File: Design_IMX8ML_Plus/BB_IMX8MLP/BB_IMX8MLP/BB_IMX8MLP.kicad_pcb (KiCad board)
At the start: 2 copper layers, 125 x 100 mm, 134 parts, among them J1 DF40C-100DP-0.4V_51_, J10 Barrel_Jack, J11 SIM_Card, J2 DF40C-100DP-0.4V_51_, J3 DF40C-100DP-0.4V_51_, J4 DF40C-100DP-0.4V_51_, J5 RJ45_Amphenol_RJMG1BD3B8K1ANR, J6 RJ45_Amphenol_RJMG1BD3B8K1ANR, J7 HDMI_A, J8 Bus_PCI_Express_Mini, J9 GSB311231HR, P1 USB_C_Plug, Q1 PMDT290UCE, Q2 NTMFS5C670NLT1G, Q3 NTMFS5C670NLT1G, Q4 PMDT290UCE, SW1 Power ON/OFF, SW2 RESET, SW3 RECOVERY, U1 KSZ9131RNXI, U10 PCMF3USB3S, U2 HDMI2C1-14HDS, U3 USB5744_2G, U4 LTC4368IDD-1_PBF, U5 AOZ2261AQI-15, U6 NCV4274CST50T3G, U7 AOZ2261AQI-15, U8 LTC2954CDDB-1-TRMPBF, U9 PCMF3USB3S, Y1 25MHz

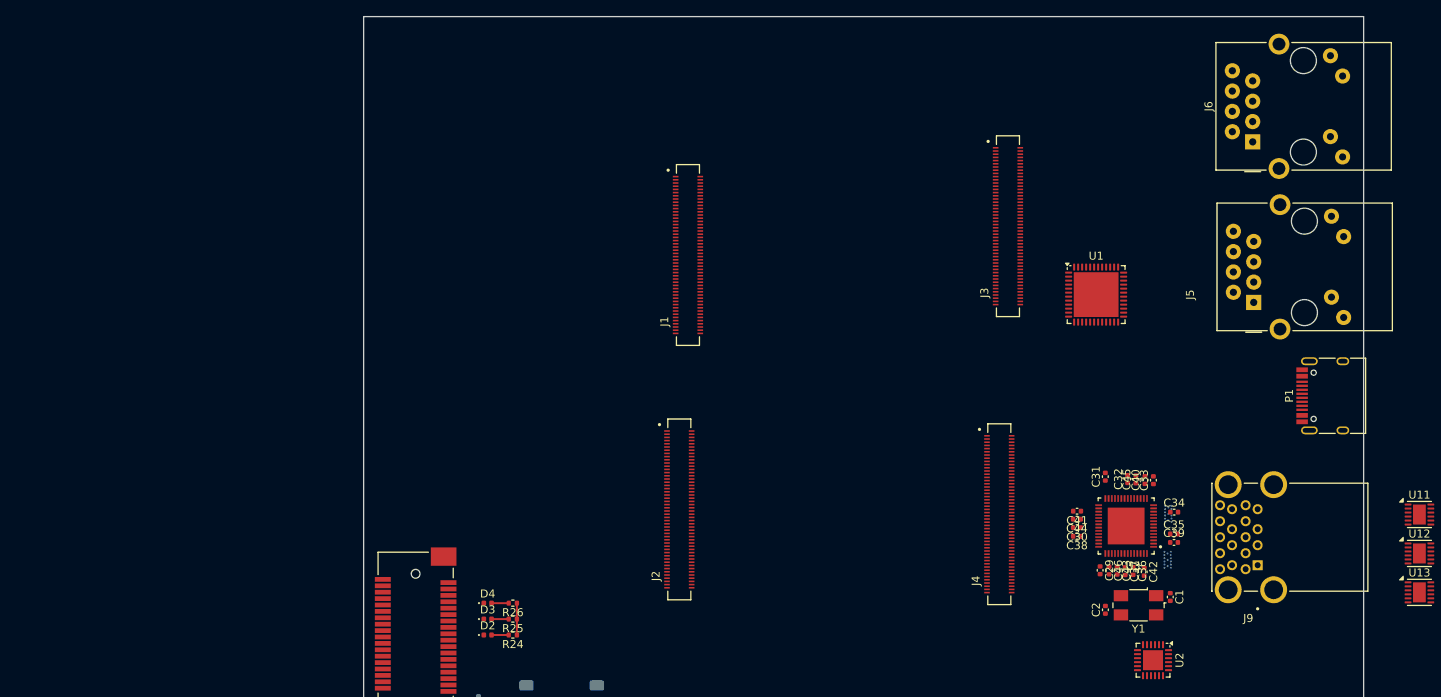
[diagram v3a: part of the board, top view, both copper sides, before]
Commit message: improving Ethernet, USB and Camera inteface
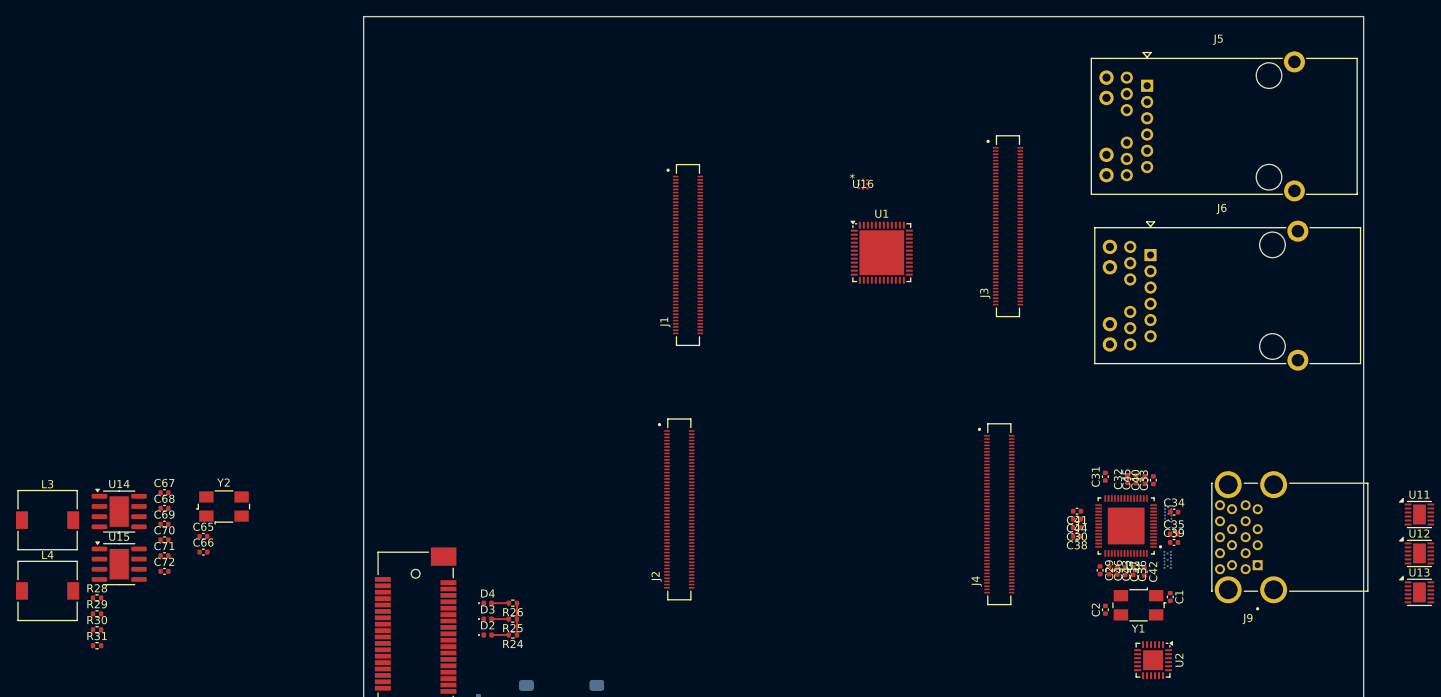
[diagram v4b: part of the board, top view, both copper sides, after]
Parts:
- removed P1: USB_C_Plug, Connector_USB:USB_C_Receptacle_HRO_TYPE-C-31-M-12
- added C65: 12Pf, Capacitor_SMD:C_0402_1005Metric, F.Cu at (50.0, 115.0)
- added C66: 12Pf, Capacitor_SMD:C_0402_1005Metric, F.Cu at (50.0, 116.9)
- added C67: 47uF, Capacitor_SMD:C_0402_1005Metric, F.Cu at (45.1, 109.5)
- added C68: 100pF, Capacitor_SMD:C_0402_1005Metric, F.Cu at (45.1, 111.5)
- added C69: 22uF, Capacitor_SMD:C_0402_1005Metric, F.Cu at (45.1, 113.4)
- added C70: 47uF, Capacitor_SMD:C_0402_1005Metric, F.Cu at (45.1, 115.4)
- added C71: 100pF, Capacitor_SMD:C_0402_1005Metric, F.Cu at (45.1, 117.4)
- added C72: 22uF, Capacitor_SMD:C_0402_1005Metric, F.Cu at (45.1, 119.3)
- added L3: 2.2uH_12A, Inductor_SMD:L_7.3x7.3_H3.5, F.Cu at (30.5, 112.9)
- added L4: 2.2uH_12A, Inductor_SMD:L_7.3x7.3_H3.5, F.Cu at (30.5, 121.8)
- added R28: 330K, Resistor_SMD:R_0402_1005Metric, F.Cu at (36.7, 122.7)
- added R29: 150K, Resistor_SMD:R_0402_1005Metric, F.Cu at (36.7, 124.7)
- added R30: 150K, Resistor_SMD:R_0402_1005Metric, F.Cu at (36.7, 126.7)
- added R31: 150K, Resistor_SMD:R_0402_1005Metric, F.Cu at (36.7, 128.6)
- added U14: ~, Package_SO:SOIC-8-1EP_3.9x4.9mm_P1.27mm_EP2.41x3.81mm, F.Cu at (39.4, 111.9)
- added U15: ~, Package_SO:SOIC-8-1EP_3.9x4.9mm_P1.27mm_EP2.41x3.81mm, F.Cu at (39.4, 118.5)
- added U16: ~, _W_SBC:MICROPAK8_1P6X1P6_ONS, F.Cu at (132.4, 71.0)
- added Y2: 25MHz, Crystal:Crystal_SMD_0603-4Pin_6.0x3.5mm, F.Cu at (52.5, 111.2)
- C17: value 47uF -> 4.7uF
- C18, C19: value 47uF -> 100nF
- C7, C8: value 100nF -> 47uF
- C9: value 4.7uF -> 47uF
- J5, J6: value RJ45_Amphenol_RJMG1BD3B8K1ANR -> RJ45_JK0654219; footprint Connector_RJ:RJ45_Amphenol_RJMG1BD3B8K1ANR -> Connector_RJ:RJ45_Pulse_JK0654219NL_Horizontal
- R1: value 47K -> 100K
- R2: value 8.87K -> 100K
- R4: value 100K -> 47K
- R5: value 100K -> 8.87K
- R6: value 510K -> 100K
- R8: value 100K -> 510K
- moved J5 30.2 mm to (167.9, 58.6), turned to 0 degrees
- moved U1 27.3 mm to (134.8, 79.5)
- moved J6 19.1 mm to (168.4, 79.8), turned to 0 degrees
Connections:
- C17 pad 1: VDD_SYS -> /power_unit/power_5v/+V_STB
- C18 pad 1: VDD_SYS -> Net-(U5B-BST)
- C18 pad 2: GND -> Net-(C18-Pad2)
- C19 pad 1: VDD_SYS -> Net-(U5A-SS)
- C21 pad 1: VDD_SYS -> +3.3V
- C22 pad 1: VDD_SYS -> +3.3V
- C23 pad 1: VDD_SYS -> +3.3V
- C24 pad 1: VDD_SYS -> +3.3V
- C25 pad 1: /power_unit/+V_STB -> /power_unit/power_3V3_1V8_1V2/+V_STB
- C7 pad 1: Net-(U5B-BST) -> VDD_SYS
- C7 pad 2: Net-(C7-Pad2) -> GND
- C8 pad 1: Net-(U5A-SS) -> VDD_SYS
- C9 pad 1: /power_unit/+V_STB -> VDD_SYS
- J5 pad 13: unconnected-(J5-SHIELD-Pad13) -> /Ethernet/ETH2_LED2
- J6 pad 13: unconnected-(J6-SHIELD-Pad13) -> ETH1_LED2
- J8 pad 11: unconnected-(J8-REFCLK--Pad11) -> PCIE_REF_PAD_CLK_N
- J8 pad 13: unconnected-(J8-REFCLK+-Pad13) -> PCIE_REF_PAD_CLK_P
- J8 pad 23: unconnected-(J8-PERn0-Pad23) -> PCIE_RXN_N
- J8 pad 25: unconnected-(J8-PERp0-Pad25) -> PCIE_RXN_P
- J8 pad 28: unconnected-(J8-+1V5-Pad28) -> Net-(J8-+1V5-Pad28)
- J8 pad 31: unconnected-(J8-PETn0-Pad31) -> PCIE_TXN_N
- J8 pad 33: unconnected-(J8-PETp0-Pad33) -> PCIE_TXN_P
- J8 pad 36: USBDN_D3- -> USBH4_D-
- J8 pad 38: USBDN_D3+ -> USBH4_D+
- J8 pad 48: unconnected-(J8-+1V5-Pad48) -> Net-(J8-+1V5-Pad28)
- J8 pad 6: unconnected-(J8-+1V5-Pad6) -> Net-(J8-+1V5-Pad28)
- J9 pad 16: unconnected-(J9B-GND_DRAIN_2-Pad16) -> GND
- L1 pad 2: Net-(C7-Pad2) -> Net-(C18-Pad2)
- L2 pad 1: VDD_SYS -> +3.3V
- Q1 pad 4: /power_unit/+V5_STB -> /power_unit/power_5v/+V5_STB
- Q4 pad 4: /power_unit/+V5_STB -> /power_unit/power_3V3_1V8_1V2/+V5_STB
- R1 pad 1: VDD_SYS -> /power_unit/power_5v/5V_EN
- R1 pad 2: /power_unit/FB_5V -> Net-(Q1B-GP)
- R16 pad 1: /power_unit/5V_EN -> /power_unit/power_3V3_1V8_1V2/5V_EN
- R17 pad 1: /power_unit/+V5_STB -> /power_unit/power_3V3_1V8_1V2/+V5_STB
- R19 pad 1: VDD_SYS -> +3.3V
- R19 pad 2: /power_unit/FB_5V -> /power_unit/power_3V3_1V8_1V2/FB_5V
- R2 pad 1: /power_unit/FB_5V -> /power_unit/power_5v/+V5_STB
- R2 pad 2: GND -> Net-(Q1B-GP)
- R20 pad 1: /power_unit/FB_5V -> /power_unit/power_3V3_1V8_1V2/FB_5V
- R22 pad 1: /power_unit/+V_SUPPLY_FILT -> /power_unit/power_3V3_1V8_1V2/+V_SUPPLY_FILT
- R23 pad 1: /power_unit/+V_STB -> /power_unit/power_3V3_1V8_1V2/+V_STB
- R3 pad 1: /power_unit/+V_STB -> Net-(Q1B-DP)
- R3 pad 2: Net-(U5B-PGOOD) -> GND
- R4 pad 1: Net-(U5A-*PFM) -> VDD_SYS
- R4 pad 2: GND -> /power_unit/power_5v/FB_5V
- R5 pad 1: Net-(Q1B-DP) -> /power_unit/power_5v/FB_5V
- R6 pad 1: /power_unit/+V_SUPPLY_FILT -> Net-(U5A-*PFM)
- R6 pad 2: Net-(U5A-TON) -> GND
- R8 pad 1: /power_unit/+V5_STB -> /power_unit/power_5v/+V_SUPPLY_FILT
- R8 pad 2: Net-(Q1B-GP) -> Net-(U5A-TON)
- R9 pad 1: /power_unit/5V_EN -> /power_unit/power_5v/+V_STB
- R9 pad 2: Net-(Q1B-GP) -> Net-(U5B-PGOOD)
- U1 pad 1: unconnected-(U1B-AVDDH-Pad1) -> Net-(U1B-AVDDH-Pad1)
- U1 pad 10: unconnected-(U1A-TXRXP_D-Pad10) -> /Ethernet/ETH2_MDI3+
- U1 pad 11: unconnected-(U1A-TXRXM_D-Pad11) -> /Ethernet/ETH2_MDI3-
- U1 pad 12: unconnected-(U1B-AVDDH-Pad12) -> Net-(U1B-AVDDH-Pad1)
- U1 pad 15: unconnected-(U1A-LED2/PHYAD1-Pad15) -> /Ethernet/ETH2_LED2
- U1 pad 17: unconnected-(U1A-LED1/PME_N1//PHYAD0-Pad17) -> /Ethernet/ETH2_LED1
- U1 pad 19: unconnected-(U1A-TXD0-Pad19) -> ENET_TD0
- U1 pad 2: unconnected-(U1A-TXRXP_A-Pad2) -> /Ethernet/ETH2_MDI0+
- U1 pad 20: unconnected-(U1A-TXD1-Pad20) -> ENET_TD1
- U1 pad 21: unconnected-(U1A-TXD2-Pad21) -> ENET_TD2
- U1 pad 22: unconnected-(U1A-TXD3-Pad22) -> ENET_TD3
- U1 pad 24: unconnected-(U1A-TXC-Pad24) -> ENET_TXC
- U1 pad 25: unconnected-(U1A-TX_CTL-Pad25) -> ENET_TX_CTL
- U1 pad 27: unconnected-(U1A-RXD3/MODE3-Pad27) -> ENET_RD3
- U1 pad 28: unconnected-(U1A-RXD2/MODE2-Pad28) -> ENET_RD2
- U1 pad 3: unconnected-(U1A-TXRXM_A-Pad3) -> /Ethernet/ETH2_MDI0-
- U1 pad 31: unconnected-(U1A-RXD1/MODE1-Pad31) -> ENET_RD1
- U1 pad 32: unconnected-(U1A-RXD0/MODE0-Pad32) -> ENET_RD0
- U1 pad 33: unconnected-(U1A-RX_CTL/CLK125_EN-Pad33) -> ENET_RX_CTL
- U1 pad 35: unconnected-(U1A-RXC/PHYAD2-Pad35) -> ENET_RXC
- U1 pad 36: unconnected-(U1A-MDC-Pad36) -> ENET_MDC
- U1 pad 37: unconnected-(U1A-MDIO-Pad37) -> ENET_MDIO
- U1 pad 4: unconnected-(U1B-AVDDL-Pad4) -> Net-(U1B-AVDDL-Pad4)
- U1 pad 42: unconnected-(U1A-RESET_N-Pad42) -> CTRL_RESET
- U1 pad 45: unconnected-(U1A-XO-Pad45) -> Net-(U1A-XO)
- U1 pad 46: unconnected-(U1A-XI-Pad46) -> Net-(U1A-XI)
- U1 pad 5: unconnected-(U1A-TXRXP_B-Pad5) -> /Ethernet/ETH2_MDI1+
- U1 pad 6: unconnected-(U1A-TXRXM_B-Pad6) -> /Ethernet/ETH2_MDI1-
- U1 pad 7: unconnected-(U1A-TXRXP_C-Pad7) -> /Ethernet/ETH2_MDI2+
- U1 pad 8: unconnected-(U1A-TXRXM_C-Pad8) -> /Ethernet/ETH2_MDI2-
- U1 pad 9: unconnected-(U1B-AVDDL-Pad9) -> Net-(U1B-AVDDL-Pad4)
- U10 pad A1: /USB/usb_connectors/USBDN_D2- -> USBH2_D-
- U10 pad A2: /USB/usb_connectors/USBDN_D2+ -> USBH2_D+
- U10 pad A3: /USB/usb_connectors/USB_SSRX_DN2- -> USBH2_SSRX-
- U10 pad A4: /USB/usb_connectors/USB_SSRX_DN2+ -> USBH2_SSRX+
- U10 pad A5: /USB/usb_connectors/USB_SSTX_DN2- -> USBH2_SSTX-
- U10 pad A6: /USB/usb_connectors/USB_SSTX_DN2+ -> USBH2_SSTX+
- U3 pad 1: /USB/USBDN_D1+ -> unconnected-(U3-USB2DN_DP1/PRT_DIS_P1-Pad1)
- U3 pad 10: /USB/USB_SSTX_DN2+ -> USBH2_SSTX+
- U3 pad 11: /USB/USB_SSTX_DN2- -> USBH2_SSTX-
- U3 pad 13: /USB/USB_SSRX_DN2+ -> USBH2_SSRX+
- U3 pad 14: /USB/USB_SSRX_DN2- -> USBH2_SSRX-
- U3 pad 17: USBDN_D3+ -> USBH3_D+
- U3 pad 18: USBDN_D3- -> USBH3_D-
- U3 pad 19: unconnected-(U3-USB3DN_TXDP3-Pad19) -> USBH3_SSTX+
- U3 pad 2: /USB/USBDN_D1- -> unconnected-(U3-USB2DN_DM1/PRT_DIS_M1-Pad2)
- U3 pad 20: unconnected-(U3-USB3DN_TXDM3-Pad20) -> USBH3_SSTX-
- U3 pad 22: unconnected-(U3-USB3DN_RXDP3-Pad22) -> USBH3_SSRX+
- U3 pad 23: unconnected-(U3-USB3DN_RXDM3-Pad23) -> USBH3_SSRX-
- U3 pad 24: /USB/USBDN_D4+ -> USBH4_D+
- U3 pad 25: /USB/USBDN_D4- -> USBH4_D-
- U3 pad 3: /USB/USB_SSTX_DN1+ -> unconnected-(U3-USB3DN_TXDP1-Pad3)
- U3 pad 34: unconnected-(U3-PRT_CTL3-Pad34) -> USBH3_PRT_CTL
- U3 pad 35: unconnected-(U3-PRT_CTL2-Pad35) -> USBH2_PRT_CTL
- U3 pad 4: /USB/USB_SSTX_DN1- -> unconnected-(U3-USB3DN_TXDM1-Pad4)
- U3 pad 6: /USB/USB_SSRX_DN1+ -> unconnected-(U3-USB3DN_RXDP1-Pad6)
- U3 pad 7: /USB/USB_SSRX_DN1- -> unconnected-(U3-USB3DN_RXDM1-Pad7)
- U3 pad 8: /USB/USBDN_D2+ -> USBH2_D+
- U3 pad 9: /USB/USBDN_D2- -> USBH2_D-
- U5 pad 10: Net-(C7-Pad2) -> Net-(C18-Pad2)
- U5 pad 11: Net-(C7-Pad2) -> Net-(C18-Pad2)
- U5 pad 16: Net-(C7-Pad2) -> Net-(C18-Pad2)
- U5 pad 17: Net-(C7-Pad2) -> Net-(C18-Pad2)
- U5 pad 18: Net-(C7-Pad2) -> Net-(C18-Pad2)
- U5 pad 21: /power_unit/+V_STB -> /power_unit/power_5v/+V_STB
- U5 pad 5: /power_unit/FB_5V -> /power_unit/power_5v/FB_5V
- U5 pad 7: /power_unit/+V_SUPPLY_FILT -> /power_unit/power_5v/+V_SUPPLY_FILT
- U5 pad 8: /power_unit/+V_SUPPLY_FILT -> /power_unit/power_5v/+V_SUPPLY_FILT
- U5 pad 9: /power_unit/+V_SUPPLY_FILT -> /power_unit/power_5v/+V_SUPPLY_FILT
- U7 pad 21: /power_unit/+V_STB -> /power_unit/power_3V3_1V8_1V2/+V_STB
- U7 pad 5: /power_unit/FB_5V -> /power_unit/power_3V3_1V8_1V2/FB_5V
- U7 pad 7: /power_unit/+V_SUPPLY_FILT -> /power_unit/power_3V3_1V8_1V2/+V_SUPPLY_FILT
- U7 pad 8: /power_unit/+V_SUPPLY_FILT -> /power_unit/power_3V3_1V8_1V2/+V_SUPPLY_FILT
- U7 pad 9: /power_unit/+V_SUPPLY_FILT -> /power_unit/power_3V3_1V8_1V2/+V_SUPPLY_FILT
- U8 pad 3: Net-(SW1-A) -> /power_unit/+V5_STB
- U9 pad A1: /USB/usb_connectors/USBDN_D1- -> USBH3_D-
- U9 pad A2: /USB/usb_connectors/USBDN_D1+ -> USBH3_D+
- U9 pad A3: /USB/usb_connectors/USB_SSTX_DN1- -> USBH3_SSTX-
- U9 pad A4: /USB/usb_connectors/USB_SSTX_DN1+ -> USBH3_SSTX+
- U9 pad A5: /USB/usb_connectors/USB_SSRX_DN1- -> USBH3_SSRX-
- U9 pad A6: /USB/usb_connectors/USB_SSRX_DN1+ -> USBH3_SSRX+
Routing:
- net GND: track 16.8 -> 30.5 mm
- net Net-(C7-Pad2): track 13.7 -> 0.00 mm
- net /power_unit/FB_5V: track 7.73 -> 0.00 mm, vias 1 -> 0
- net Net-(Q1B-GP): track 8.71 -> 16.4 mm, vias 0 -> 1
- net /power_unit/+V_STB: track 2.70 -> 0.00 mm
- net (no net): track 0.00 -> 2.70 mm

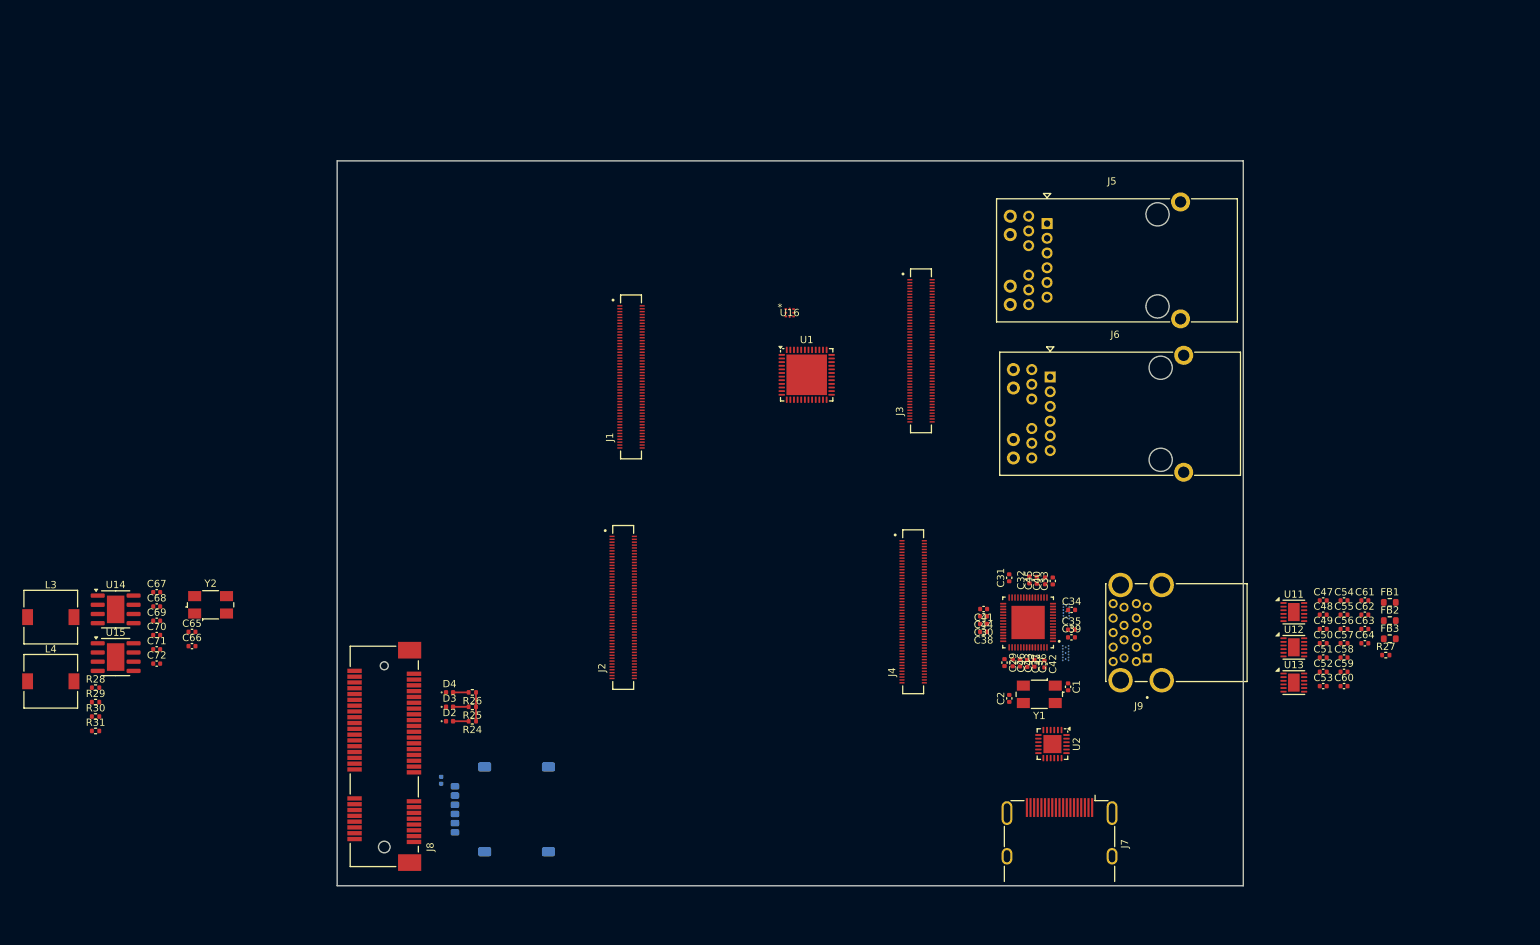
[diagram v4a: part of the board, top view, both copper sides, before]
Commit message: Add LVDs and CSI Interface
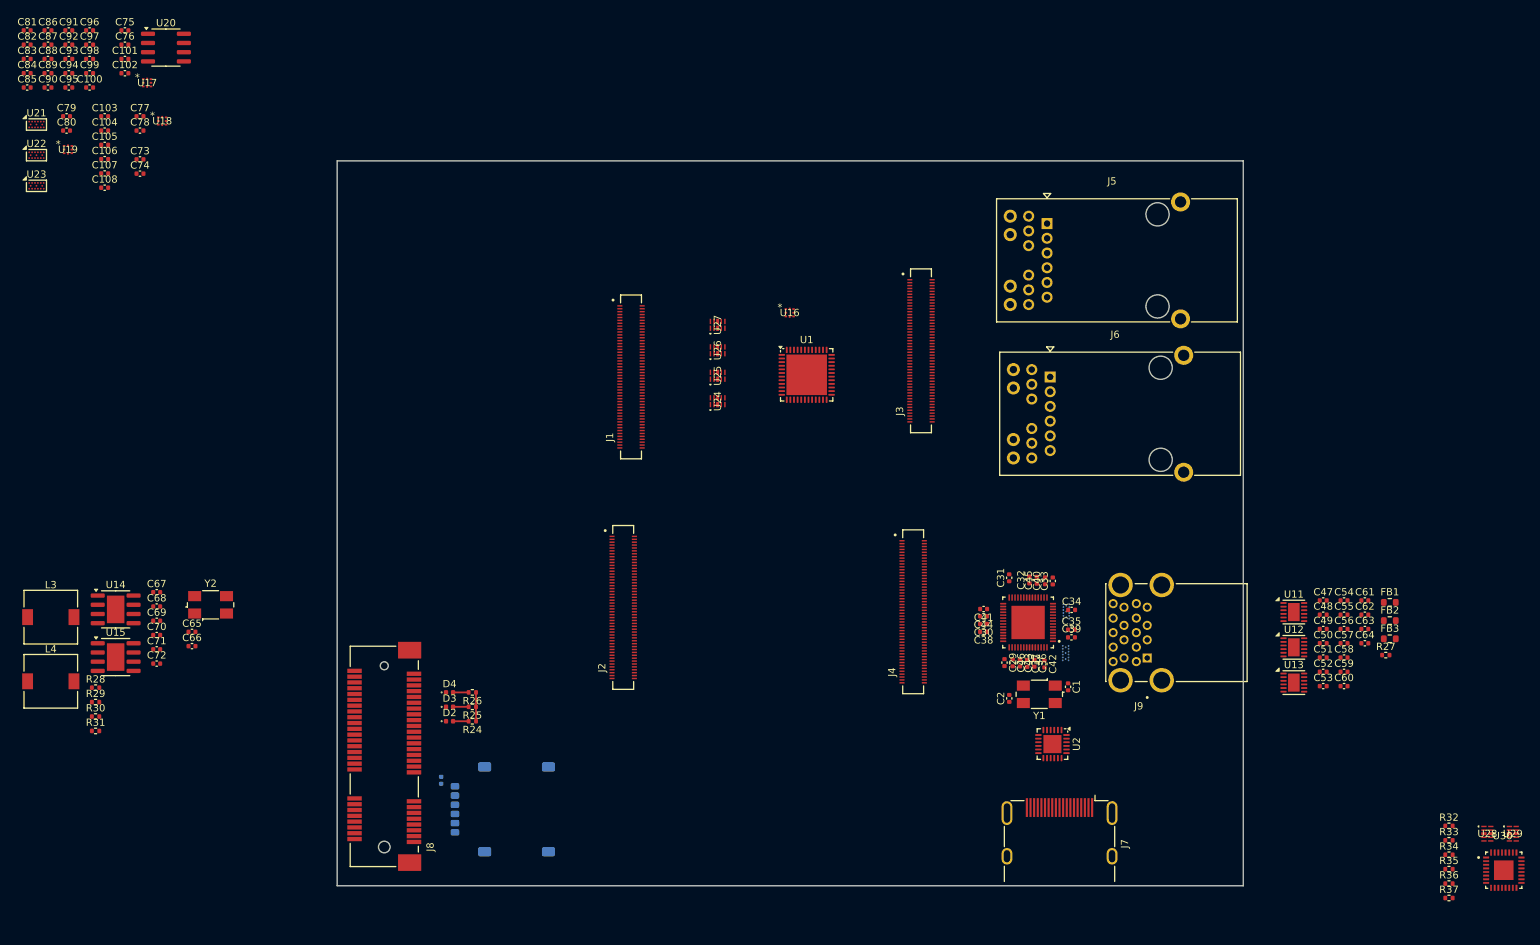
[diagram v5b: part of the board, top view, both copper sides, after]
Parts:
- added C100: 100nF, Capacitor_SMD:C_0402_1005Metric, F.Cu at (35.9, 39.9)
- added C101: 100nF, Capacitor_SMD:C_0402_1005Metric, F.Cu at (40.7, 35.9)
- added C102: 100nF, Capacitor_SMD:C_0402_1005Metric, F.Cu at (40.7, 37.9)
- added C103: 22uF, Capacitor_SMD:C_0402_1005Metric, F.Cu at (37.9, 43.9)
- added C104: 4,7uF, Capacitor_SMD:C_0402_1005Metric, F.Cu at (37.9, 45.8)
- added C105: 4,7uF, Capacitor_SMD:C_0402_1005Metric, F.Cu at (37.9, 47.8)
- added C106: 4,7uF, Capacitor_SMD:C_0402_1005Metric, F.Cu at (37.9, 49.8)
- added C107: 4,7uF, Capacitor_SMD:C_0402_1005Metric, F.Cu at (37.9, 51.7)
- added C108: 4,7uF, Capacitor_SMD:C_0402_1005Metric, F.Cu at (37.9, 53.7)
- added C73: 100nF, Capacitor_SMD:C_0402_1005Metric, F.Cu at (42.8, 49.8)
- added C74: 100nF, Capacitor_SMD:C_0402_1005Metric, F.Cu at (42.8, 51.8)
- added C75: 100nF, Capacitor_SMD:C_0402_1005Metric, F.Cu at (40.7, 32.0)
- added C76: 100nF, Capacitor_SMD:C_0402_1005Metric, F.Cu at (40.7, 34.0)
- added C77: 100nF, Capacitor_SMD:C_0402_1005Metric, F.Cu at (42.8, 43.9)
- added C78: 100nF, Capacitor_SMD:C_0402_1005Metric, F.Cu at (42.8, 45.8)
- added C79: 100nF, Capacitor_SMD:C_0402_1005Metric, F.Cu at (32.7, 43.9)
- added C80: 100nF, Capacitor_SMD:C_0402_1005Metric, F.Cu at (32.7, 45.8)
- added C81: 10uF, Capacitor_SMD:C_0402_1005Metric, F.Cu at (27.2, 32.0)
- added C82: 100nF, Capacitor_SMD:C_0402_1005Metric, F.Cu at (27.2, 34.0)
- added C83: 100nF, Capacitor_SMD:C_0402_1005Metric, F.Cu at (27.2, 35.9)
- added C84: 100nF, Capacitor_SMD:C_0402_1005Metric, F.Cu at (27.2, 37.9)
- added C85: 100nF, Capacitor_SMD:C_0402_1005Metric, F.Cu at (27.2, 39.9)
- added C86: 100nF, Capacitor_SMD:C_0402_1005Metric, F.Cu at (30.1, 32.0)
- added C87: 100nF, Capacitor_SMD:C_0402_1005Metric, F.Cu at (30.1, 34.0)
- added C88: 100nF, Capacitor_SMD:C_0402_1005Metric, F.Cu at (30.1, 35.9)
- added C89: 100nF, Capacitor_SMD:C_0402_1005Metric, F.Cu at (30.1, 37.9)
- added C90: 100nF, Capacitor_SMD:C_0402_1005Metric, F.Cu at (30.1, 39.9)
- added C91: 10uF, Capacitor_SMD:C_0402_1005Metric, F.Cu at (33.0, 32.0)
- added C92: 100nF, Capacitor_SMD:C_0402_1005Metric, F.Cu at (33.0, 34.0)
- added C93: 100nF, Capacitor_SMD:C_0402_1005Metric, F.Cu at (33.0, 35.9)
- added C94: 100nF, Capacitor_SMD:C_0402_1005Metric, F.Cu at (33.0, 37.9)
- added C95: 10uF, Capacitor_SMD:C_0402_1005Metric, F.Cu at (33.0, 39.9)
- added C96: 100nF, Capacitor_SMD:C_0402_1005Metric, F.Cu at (35.9, 32.0)
- added C97: 100nF, Capacitor_SMD:C_0402_1005Metric, F.Cu at (35.9, 34.0)
- added C98: 100nF, Capacitor_SMD:C_0402_1005Metric, F.Cu at (35.9, 35.9)
- added C99: 10uF, Capacitor_SMD:C_0402_1005Metric, F.Cu at (35.9, 37.9)
- added R32: 1K, Resistor_SMD:R_0402_1005Metric, F.Cu at (223.4, 141.7)
- added R33: 1K, Resistor_SMD:R_0402_1005Metric, F.Cu at (223.4, 143.7)
- added R34: 200K, Resistor_SMD:R_0402_1005Metric, F.Cu at (223.4, 145.7)
- added R35: 200K, Resistor_SMD:R_0402_1005Metric, F.Cu at (223.4, 147.7)
- added R36: 1K, Resistor_SMD:R_0402_1005Metric, F.Cu at (223.4, 149.7)
- added R37: 12K, Resistor_SMD:R_0402_1005Metric, F.Cu at (223.4, 151.7)
- added U17: FXMA2102L8X, _W_SBC:MICROPAK8_1P6X1P6_ONS, F.Cu at (43.8, 39.2)
- added U18: ~, _W_SBC:MICROPAK8_1P6X1P6_ONS, F.Cu at (45.9, 44.5)
- added U19: ~, _W_SBC:MICROPAK8_1P6X1P6_ONS, F.Cu at (32.9, 48.4)
- added U20: INA219BxD, Package_SO:SOIC-8_3.9x4.9mm_P1.27mm, F.Cu at (46.4, 34.4)
- added U21: PCMF3USB3S, Package_CSP:Nexperia_WLCSP-15_6-3-6_2.37x1.17mm_Layout6x3_P0.4mm, F.Cu at (28.5, 45.0)
- added U22: PCMF3USB3S, Package_CSP:Nexperia_WLCSP-15_6-3-6_2.37x1.17mm_Layout6x3_P0.4mm, F.Cu at (28.5, 49.2)
- added U23: PCMF3USB3S, Package_CSP:Nexperia_WLCSP-15_6-3-6_2.37x1.17mm_Layout6x3_P0.4mm, F.Cu at (28.5, 53.4)
- added U24: ~, _W_SBC:DFN10_U-DFN2510-10_DIO, F.Cu at (122.5, 83.2)
- added U25: ~, _W_SBC:DFN10_U-DFN2510-10_DIO, F.Cu at (122.5, 79.6)
- added U26: ~, _W_SBC:DFN10_U-DFN2510-10_DIO, F.Cu at (122.5, 76.1)
- added U27: ~, _W_SBC:DFN10_U-DFN2510-10_DIO, F.Cu at (122.5, 72.6)
- added U28: ~, _W_SBC:DFN10_U-DFN2510-10_DIO, F.Cu at (228.7, 142.8)
- added U29: ~, _W_SBC:DFN10_U-DFN2510-10_DIO, F.Cu at (232.2, 142.8)
- added U30: NAU88C22YG, _W_SBC:QFN50P500X500X80-33N, F.Cu at (230.9, 147.8)
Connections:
- net Net-(J8-+1V5-Pad28) renamed /PCIe/1V5_PCIe
- net Net-(J8-+3V3AUX-Pad2) renamed /PCIe/3V3_PCIe
- net Net-(U1B-AVDDH-Pad1) renamed /Ethernet/3v3
- net Net-(U1B-DVDDH-Pad16) renamed /Ethernet/1v8
- C1 pad 2: GND -> LVDS0_D2_N
- C10 pad 2: GND -> LVDS0_D2_N
- C11 pad 2: GND -> LVDS0_D2_N
- C12 pad 2: GND -> LVDS0_D2_N
- C13 pad 2: GND -> LVDS0_D2_N
- C14 pad 2: GND -> LVDS0_D2_N
- C15 pad 2: GND -> LVDS0_D2_N
- C16 pad 2: GND -> LVDS0_D2_N
- C17 pad 2: GND -> LVDS0_D2_N
- C19 pad 2: GND -> LVDS0_D2_N
- C2 pad 2: GND -> LVDS0_D2_N
- C20 pad 2: GND -> LVDS0_D2_N
- C21 pad 2: GND -> LVDS0_D2_N
- C22 pad 2: GND -> LVDS0_D2_N
- C23 pad 2: GND -> LVDS0_D2_N
- C24 pad 2: GND -> LVDS0_D2_N
- C25 pad 2: GND -> LVDS0_D2_N
- C27 pad 2: GND -> LVDS0_D2_N
- C28 pad 2: GND -> LVDS0_D2_N
- C29 pad 2: GND -> LVDS0_D2_N
- C3 pad 2: GND -> LVDS0_D2_N
- C30 pad 2: GND -> LVDS0_D2_N
- C31 pad 2: GND -> LVDS0_D2_N
- C32 pad 2: GND -> LVDS0_D2_N
- C33 pad 2: GND -> LVDS0_D2_N
- C34 pad 2: GND -> LVDS0_D2_N
- C35 pad 2: GND -> LVDS0_D2_N
- C36 pad 2: GND -> LVDS0_D2_N
- C37 pad 2: GND -> LVDS0_D2_N
- C38 pad 2: GND -> LVDS0_D2_N
- C39 pad 2: GND -> LVDS0_D2_N
- C4 pad 2: GND -> LVDS0_D2_N
- C40 pad 2: GND -> LVDS0_D2_N
- C41 pad 2: GND -> LVDS0_D2_N
- C42 pad 2: GND -> LVDS0_D2_N
- C43 pad 2: GND -> LVDS0_D2_N
- C44 pad 2: GND -> LVDS0_D2_N
- C45 pad 2: GND -> LVDS0_D2_N
- C46 pad 2: GND -> LVDS0_D2_N
- C47 pad 2: GND -> LVDS0_D2_N
- C48 pad 2: GND -> LVDS0_D2_N
- C49 pad 2: GND -> LVDS0_D2_N
- C5 pad 2: GND -> LVDS0_D2_N
- C50 pad 2: GND -> LVDS0_D2_N
- C51 pad 2: GND -> LVDS0_D2_N
- C52 pad 2: GND -> LVDS0_D2_N
- C53 pad 2: GND -> LVDS0_D2_N
- C54 pad 2: GND -> LVDS0_D2_N
- C55 pad 2: GND -> LVDS0_D2_N
- C56 pad 2: GND -> LVDS0_D2_N
- C57 pad 2: GND -> LVDS0_D2_N
- C58 pad 2: GND -> LVDS0_D2_N
- C59 pad 2: GND -> LVDS0_D2_N
- C6 pad 2: GND -> LVDS0_D2_N
- C60 pad 2: GND -> LVDS0_D2_N
- C61 pad 2: GND -> LVDS0_D2_N
- C62 pad 2: GND -> LVDS0_D2_N
- C63 pad 2: GND -> LVDS0_D2_N
- C64 pad 2: GND -> LVDS0_D2_N
- C65 pad 2: GND -> LVDS0_D2_N
- C66 pad 2: GND -> LVDS0_D2_N
- C67 pad 2: GND -> LVDS0_D2_N
- C69 pad 2: GND -> LVDS0_D2_N
- C7 pad 2: GND -> LVDS0_D2_N
- C70 pad 2: GND -> LVDS0_D2_N
- C72 pad 2: GND -> LVDS0_D2_N
- C8 pad 2: GND -> LVDS0_D2_N
- C9 pad 2: GND -> LVDS0_D2_N
- D1 pad 2: GND -> LVDS0_D2_N
- J10 pad 2: GND -> LVDS0_D2_N
- J11 pad 5: GND -> LVDS0_D2_N
- J3 pad 75: GND -> LVDS0_D2_N
- J3 pad 76: GND -> LVDS0_D2_N
- J3 pad 77: GND -> LVDS0_D2_N
- J3 pad 78: GND -> LVDS0_D2_N
- J3 pad 79: GND -> LVDS0_D2_N
- J3 pad 80: GND -> LVDS0_D2_N
- J3 pad 81: GND -> LVDS0_D2_N
- J3 pad 82: GND -> LVDS0_D2_N
- J3 pad 83: GND -> LVDS0_D2_N
- J3 pad 84: GND -> LVDS0_D2_N
- J3 pad 85: GND -> LVDS0_D2_N
- J3 pad 86: GND -> LVDS0_D2_N
- J3 pad 87: GND -> LVDS0_D2_N
- J3 pad 88: GND -> LVDS0_D2_N
- J4 pad 47: LVDS1_D2_N -> LVDS0_D2_N
- J8 pad 30: unconnected-(J8-SMB_CLK-Pad30) -> /PCIe/PCIe_CLK
- J8 pad 32: unconnected-(J8-SMB_DATA-Pad32) -> /PCIe/PCIe_SDA
- J9 pad 13: GND -> LVDS0_D2_N
- J9 pad 16: GND -> LVDS0_D2_N
- J9 pad 4: GND -> LVDS0_D2_N
- J9 pad 7: GND -> LVDS0_D2_N
- R13 pad 2: GND -> LVDS0_D2_N
- R18 pad 2: GND -> LVDS0_D2_N
- R20 pad 2: GND -> LVDS0_D2_N
- R21 pad 2: GND -> LVDS0_D2_N
- R29 pad 2: GND -> LVDS0_D2_N
- R3 pad 2: GND -> LVDS0_D2_N
- R31 pad 2: GND -> LVDS0_D2_N
- R5 pad 2: GND -> LVDS0_D2_N
- R6 pad 2: GND -> LVDS0_D2_N
- SW1 pad 1: GND -> LVDS0_D2_N
- SW1 pad 2: GND -> LVDS0_D2_N
- SW2 pad 1: GND -> LVDS0_D2_N
- SW2 pad 2: GND -> LVDS0_D2_N
- SW3 pad 1: GND -> LVDS0_D2_N
- SW3 pad 2: GND -> LVDS0_D2_N
- U1 pad 18: Net-(U1B-DVDDL-Pad18) -> /Ethernet/1v2
- U1 pad 23: Net-(U1B-DVDDL-Pad18) -> /Ethernet/1v2
- U1 pad 26: Net-(U1B-DVDDL-Pad18) -> /Ethernet/1v2
- U1 pad 29: GND -> LVDS0_D2_N
- U1 pad 30: Net-(U1B-DVDDL-Pad18) -> /Ethernet/1v2
- U1 pad 39: Net-(U1B-DVDDL-Pad18) -> /Ethernet/1v2
- U1 pad 4: Net-(U1B-AVDDL-Pad4) -> /Ethernet/1v2
- U1 pad 44: unconnected-(U1B-AVDDL_PLL-Pad44) -> /Ethernet/1v2
- U1 pad 49: GND -> LVDS0_D2_N
- U1 pad 9: Net-(U1B-AVDDL-Pad4) -> /Ethernet/1v2
- U10 pad B1: GND -> LVDS0_D2_N
- U10 pad B2: GND -> LVDS0_D2_N
- U10 pad B3: GND -> LVDS0_D2_N
- U11 pad 13: GND -> LVDS0_D2_N
- U11 pad 7: GND -> LVDS0_D2_N
- U12 pad 13: GND -> LVDS0_D2_N
- U12 pad 7: GND -> LVDS0_D2_N
- U13 pad 13: GND -> LVDS0_D2_N
- U13 pad 7: GND -> LVDS0_D2_N
- U14 pad 4: GND -> LVDS0_D2_N
- U15 pad 4: GND -> LVDS0_D2_N
- U16 pad 1: unconnected-(U16-VCCA-Pad1) -> Net-(U16-VCCA)
- U16 pad 4: unconnected-(U16-GND-Pad4) -> LVDS0_D2_N
- U16 pad 8: unconnected-(U16-VCCB-Pad8) -> Net-(U16-VCCB)
- U3 pad 1: unconnected-(U3-USB2DN_DP1/PRT_DIS_P1-Pad1) -> Net-(U3-USB2DN_DP1/PRT_DIS_P1)
- U3 pad 2: unconnected-(U3-USB2DN_DM1/PRT_DIS_M1-Pad2) -> Net-(U3-USB2DN_DM1/PRT_DIS_M1)
- U3 pad 38: unconnected-(U3-SPI_CLK/SMCLK/GPIO4-Pad38) -> /USB/I2C1_USBH_SCL
- U3 pad 39: unconnected-(U3-SPI_DO/SMDAT/GPIO5-Pad39) -> /USB/I2C1_USBH_SDA
- U3 pad 40: unconnected-(U3-SPI_DI/CFG_BC_EN/GPIO9-Pad40) -> Net-(U3-SPI_DI/CFG_BC_EN/GPIO9)
- U3 pad 41: unconnected-(U3-SPI_CE_N/CFG_NON_REM/GPIO7-Pad41) -> Net-(U3-SPI_CE_N/CFG_NON_REM/GPIO7)
- U3 pad 42: unconnected-(U3-RESET_N-Pad42) -> CTRL_RESET
- U3 pad 52: unconnected-(U3-ATEST-Pad52) -> Net-(U3-ATEST)
- U3 pad 56: unconnected-(U3-RBIAS-Pad56) -> Net-(U3-RBIAS)
- U3 pad 57: GND -> LVDS0_D2_N
- U4 pad 11: GND -> LVDS0_D2_N
- U4 pad 5: GND -> LVDS0_D2_N
- U5 pad 12: GND -> LVDS0_D2_N
- U5 pad 13: GND -> LVDS0_D2_N
- U5 pad 14: GND -> LVDS0_D2_N
- U5 pad 15: GND -> LVDS0_D2_N
- U5 pad 19: GND -> LVDS0_D2_N
- U5 pad 4: GND -> LVDS0_D2_N
- U6 pad 2: GND -> LVDS0_D2_N
- U6 pad 4: GND -> LVDS0_D2_N
- U7 pad 12: GND -> LVDS0_D2_N
- U7 pad 13: GND -> LVDS0_D2_N
- U7 pad 14: GND -> LVDS0_D2_N
- U7 pad 15: GND -> LVDS0_D2_N
- U7 pad 19: GND -> LVDS0_D2_N
- U7 pad 4: GND -> LVDS0_D2_N
- U8 pad 1: GND -> LVDS0_D2_N
- U8 pad 9: GND -> LVDS0_D2_N
- U9 pad B1: GND -> LVDS0_D2_N
- U9 pad B2: GND -> LVDS0_D2_N
- U9 pad B3: GND -> LVDS0_D2_N
- Y1 pad 2: GND -> LVDS0_D2_N
- Y1 pad 4: GND -> LVDS0_D2_N
- Y2 pad 2: GND -> LVDS0_D2_N
- Y2 pad 4: GND -> LVDS0_D2_N
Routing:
- net GND: track 30.5 -> 0.00 mm, vias 2 -> 0
- net (no net): track 2.70 -> 24.1 mm
- net LVDS0_D2_N: track 0.00 -> 9.10 mm, vias 0 -> 2
